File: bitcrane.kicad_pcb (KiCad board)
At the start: 4 copper layers, 110 x 100 mm, 110 parts, among them J1 0455580003, J10 PSU Comm, J11 0353180420, J12 0353180420, J13 0353180420, J14 0353180420, J15 Conn_01x04, J2 USB_C_Receptacle_USB2.0, J3 2x9P 2mm, J4 2x9P 2mm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

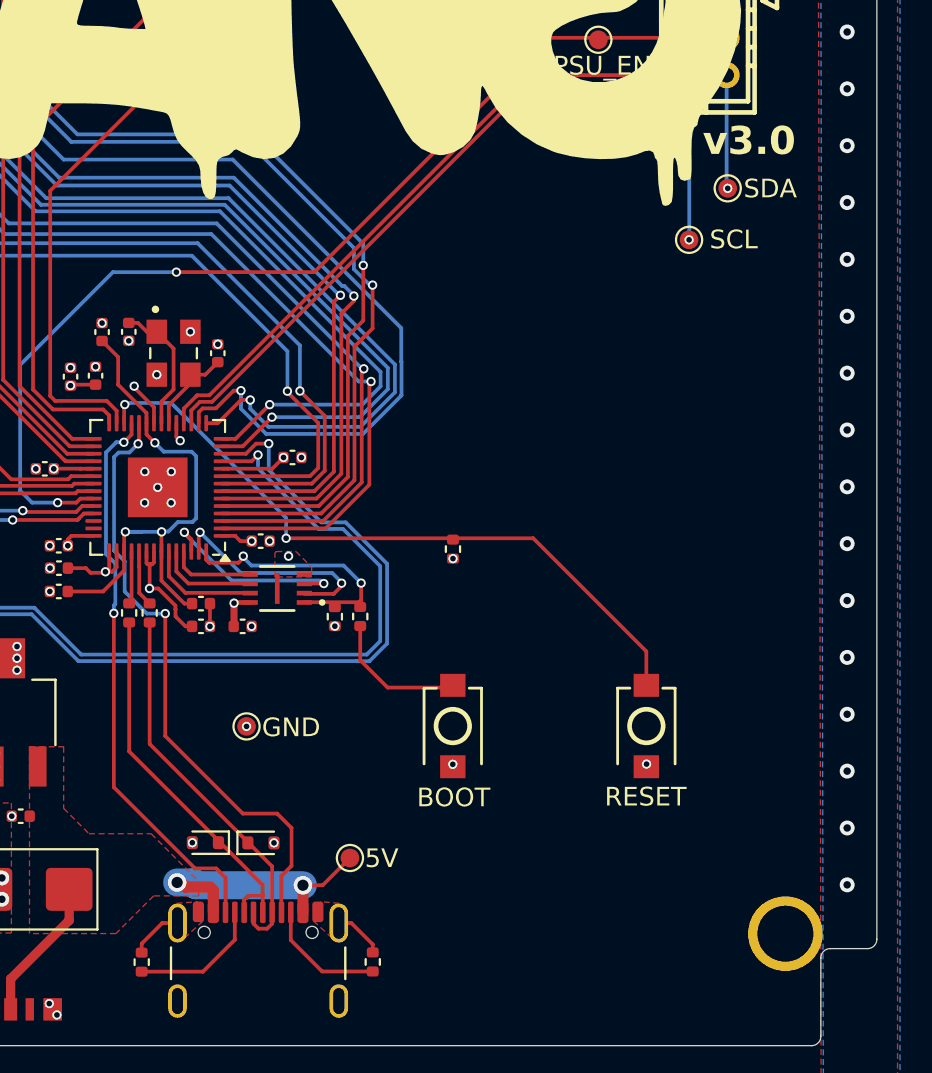
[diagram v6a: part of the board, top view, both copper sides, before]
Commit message: add SWD header for #14
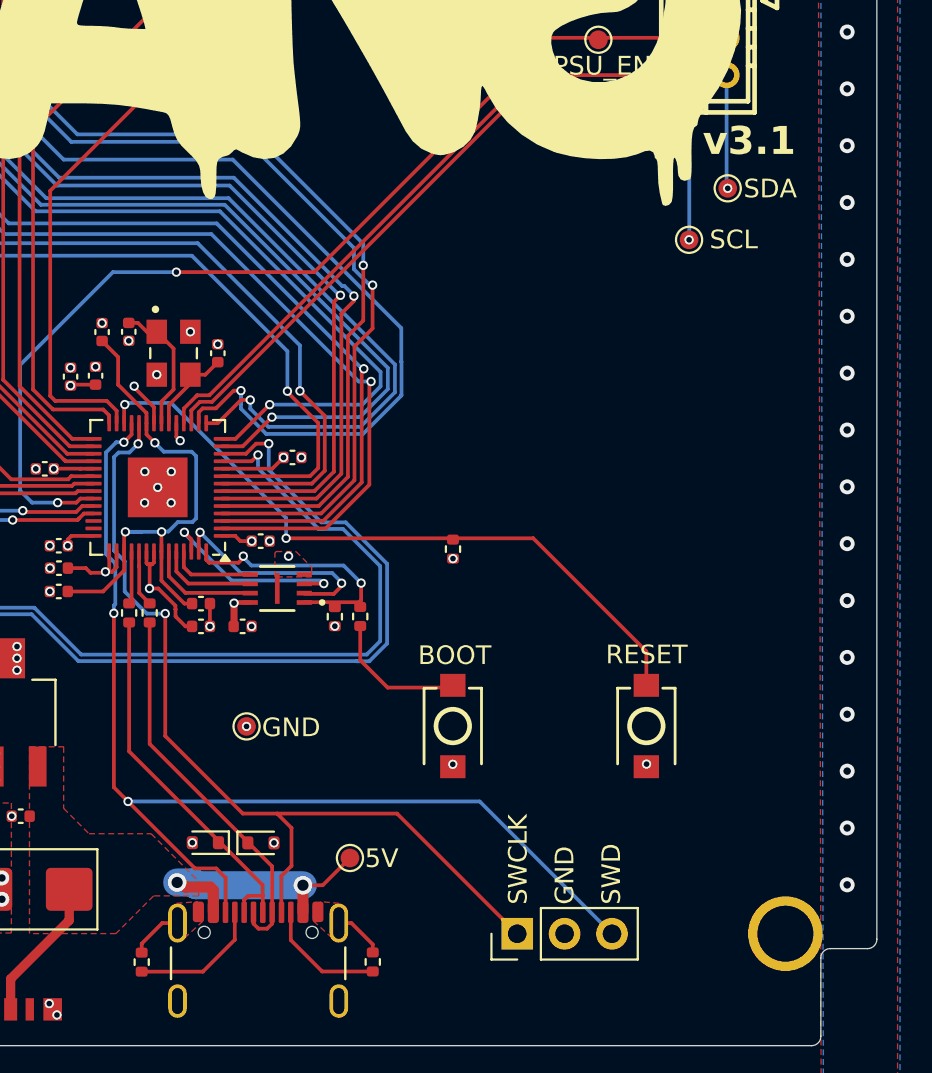
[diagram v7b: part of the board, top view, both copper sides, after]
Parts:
- added J16: Conn_01x03, Connector_PinHeader_2.54mm:PinHeader_1x03_P2.54mm_Vertical, F.Cu at (149.0, 128.2)
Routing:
- net /SWD: track 30.4 -> 59.3 mm, vias 2 -> 3
- net /SWCLK: track 32.9 -> 48.4 mm
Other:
- board text added: "GND"
- board text added: "SWCLK"
- board text added: "SWD"
- board text added: "v3.1"
- board text removed: "v3.0"
